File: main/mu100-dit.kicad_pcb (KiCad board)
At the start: 2 copper layers, 17.6 x 40 mm, 16 parts, among them J1 Conn_01x10_Female, U1 TOTX-177L, U2 AK4103A

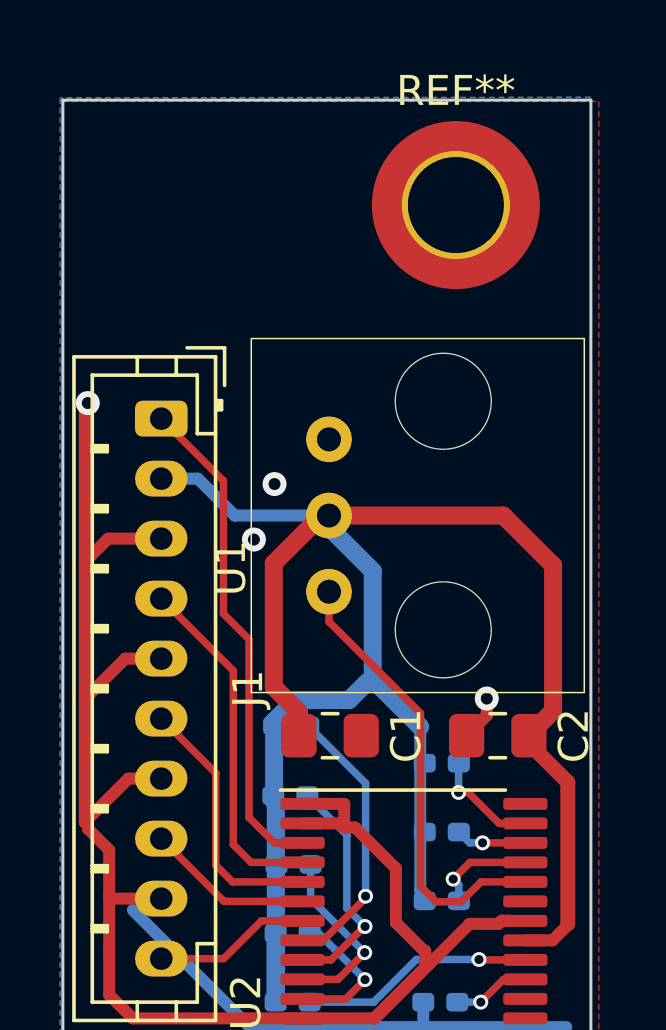
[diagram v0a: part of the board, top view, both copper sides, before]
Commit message: Add reset circuit, remove need for reset
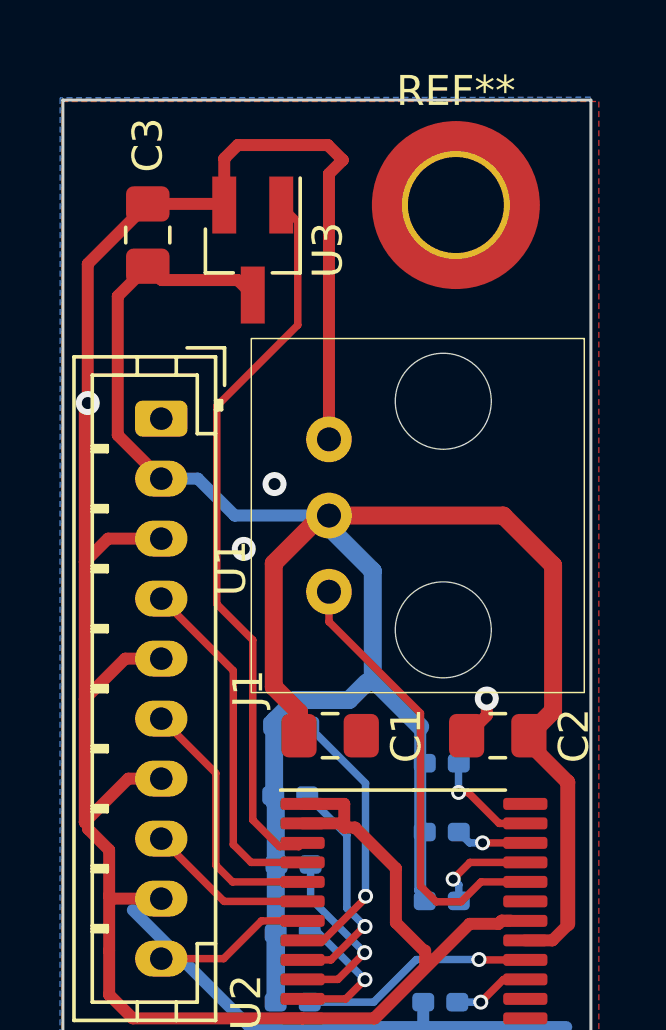
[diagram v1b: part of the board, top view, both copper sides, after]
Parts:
- added C3: 0.1u/35V, Capacitor_SMD:C_0805_2012Metric_Pad1.18x1.45mm_HandSolder, F.Cu at (46.5, 90.5)
- added U3: APX809S-46SR-7, Package_TO_SOT_SMD:SOT-23_Handsoldering, F.Cu at (50.0, 91.0)
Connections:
- J1 pad 1: /RESET -> unconnected-(J1-Pad1)
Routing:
- net GND: track 76.6 -> 107.3 mm
- net +5V: track 65.9 -> 77.9 mm
- net /RESET: track 16.6 -> 24.4 mm
- net /LRCK: track 5.23 -> 0.00 mm

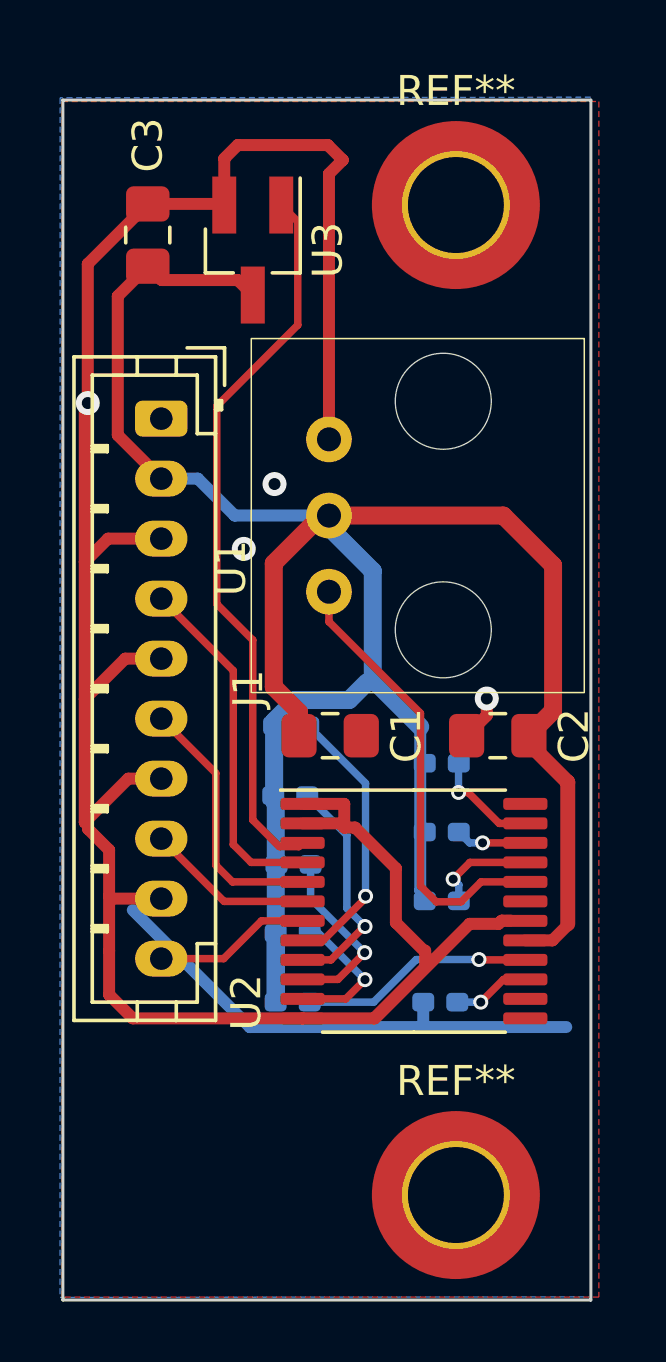
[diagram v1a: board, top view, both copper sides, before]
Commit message: Update screw hole position
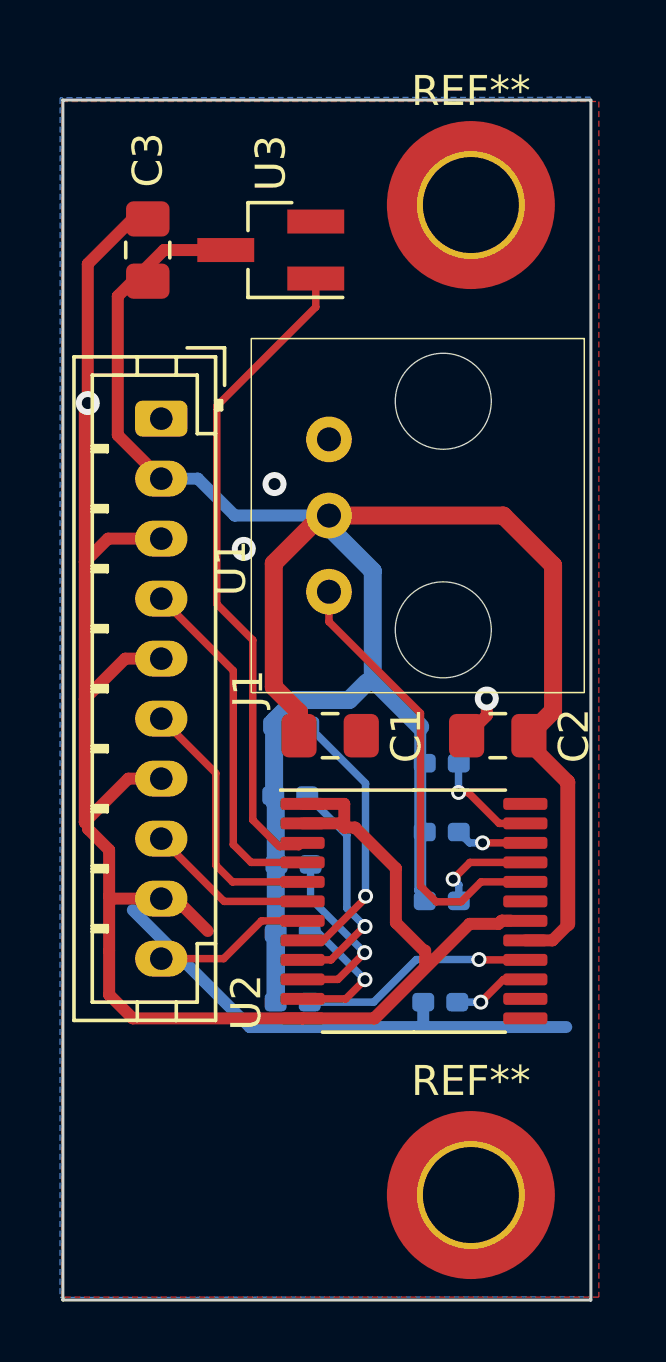
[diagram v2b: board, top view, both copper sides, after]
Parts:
- moved U3 0.60 mm to (50.6, 91.0), turned to 180 degrees
- moved C3 0.50 mm to (46.5, 91.0)
- moved REF** 0.50 mm to (57.3, 89.5)
- moved REF** 0.50 mm to (57.3, 122.5)
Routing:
- net GND: track 107.3 -> 91.0 mm
- net /RESET: track 24.4 -> 22.0 mm
- net +5V: track 77.9 -> 76.9 mm

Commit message: Move reset circuit to other side of board
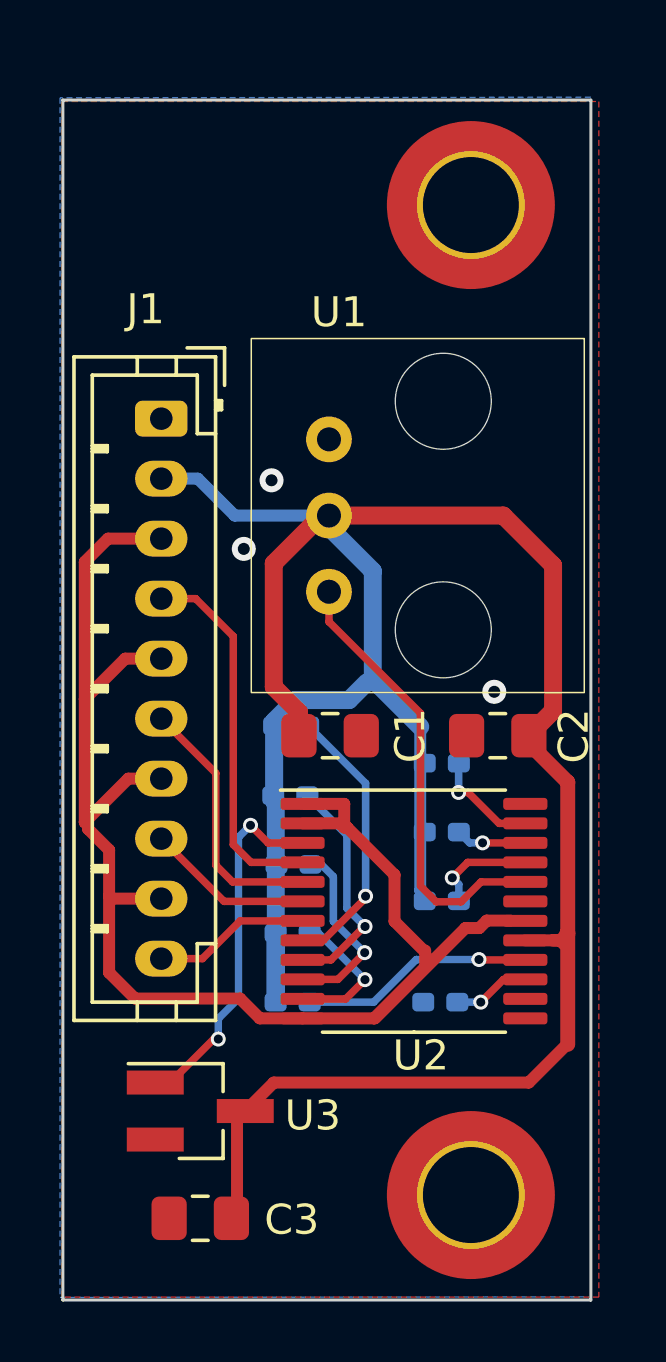
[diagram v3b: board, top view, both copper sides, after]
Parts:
- moved C3 32.3 mm to (48.2, 123.3), turned to 0 degrees
- moved U3 28.8 mm to (48.2, 119.7), turned to 0 degrees
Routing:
- net GND: track 91.0 -> 52.4 mm, vias 4 -> 3
- net +5V: track 76.9 -> 89.0 mm
- net /RESET: track 22.0 -> 12.2 mm, vias 0 -> 2
- net /LRCK: track 0.00 -> 5.23 mm
- net /MCLK: track 11.7 -> 12.4 mm

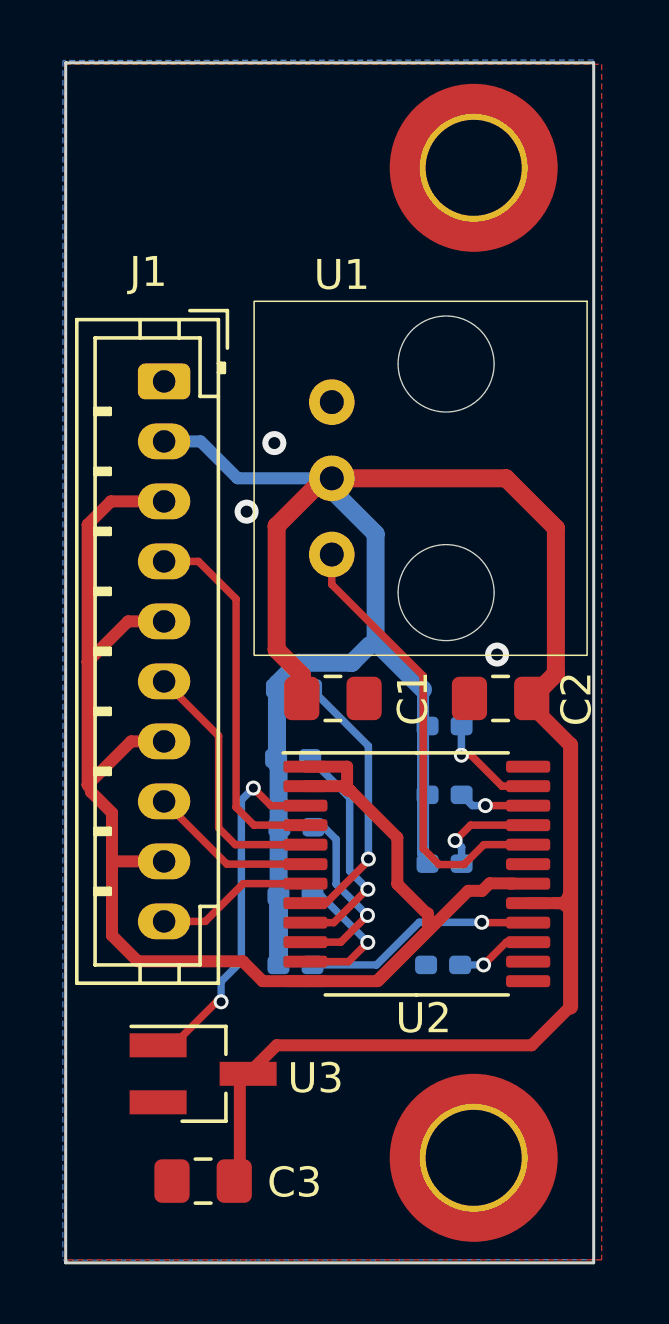
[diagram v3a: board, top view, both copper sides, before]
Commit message: Add header for optional coax output
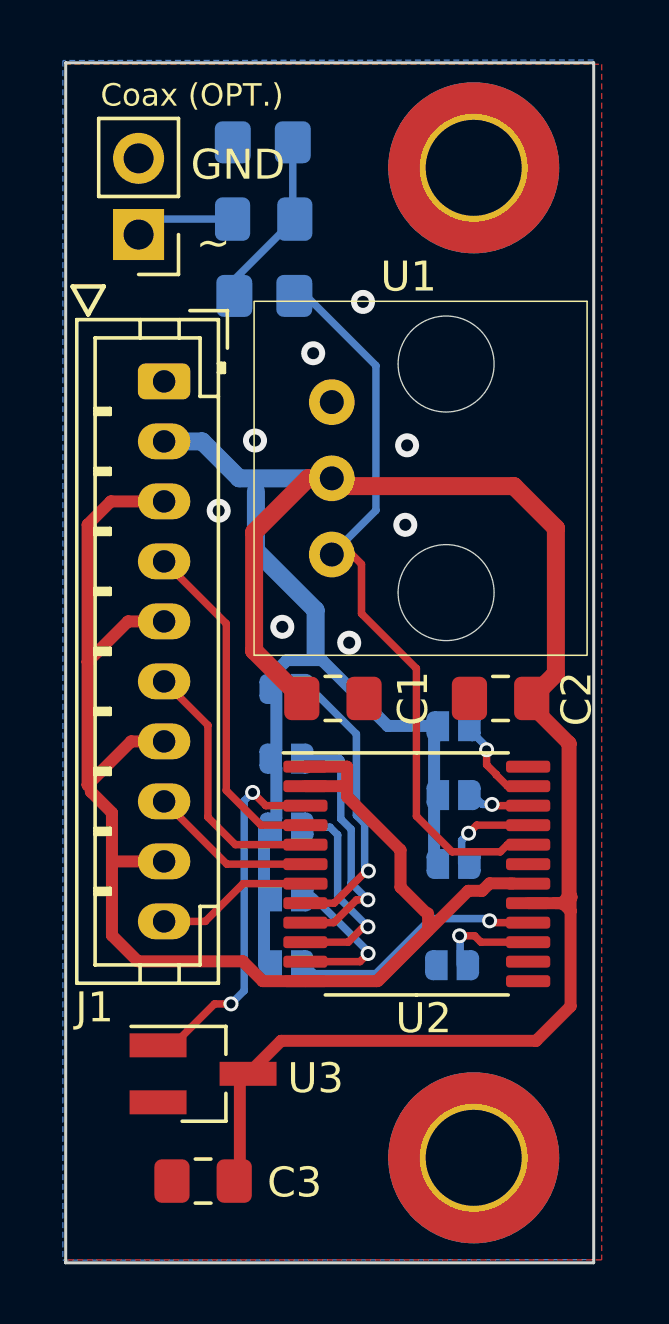
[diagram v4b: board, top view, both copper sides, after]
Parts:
- added C4: 0.1u/35V, Capacitor_SMD:C_0805_2012Metric_Pad1.18x1.45mm_HandSolder, B.Cu at (50.3, 91.2)
- added J2: Conn_01x02_Male, Connector_PinHeader_2.54mm:PinHeader_1x02_P2.54mm_Vertical, F.Cu at (46.1, 91.7)
- added R1: 330, Resistor_SMD:R_0805_2012Metric_Pad1.20x1.40mm_HandSolder, B.Cu at (50.3, 93.8)
- added R2: 100, Resistor_SMD:R_0805_2012Metric_Pad1.20x1.40mm_HandSolder, B.Cu at (50.2, 88.7)
- H1, H2: renamed from REF**; value MountingHole_3.2mm_M3_DIN965_Pad_TopOnly -> MountingHole_Pad; footprint MountingHole:MountingHole_3.2mm_M3_DIN965_Pad_TopOnly -> MountingHole:MountingHole_3.2mm_M3_ISO7380_Pad_TopBottom
- JP1, JP2, JP3, JP4, JP5, JP6, JP7, JP8, JP9: footprint Capacitor_SMD:C_0402_1005Metric_Pad0.74x0.62mm_HandSolder -> footprints:SolderJumper-Open_RoundedPad-custom
- moved JP3 0.33 mm to (51.0, 111.5)
- moved JP5 0.30 mm to (56.6, 112.7)
- moved JP6 0.30 mm to (56.6, 110.4)
- moved JP7 0.30 mm to (56.6, 108.1)
- moved JP4 0.30 mm to (51.0, 113.8)
- moved JP8 0.30 mm to (56.5, 116.1)
- moved JP9 0.30 mm to (51.0, 116.1)
- moved JP1 0.25 mm to (51.0, 106.9)
- moved JP2 0.22 mm to (51.0, 109.2)
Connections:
- H1 pad 1: (no net) -> GND
- H2 pad 1: (no net) -> GND
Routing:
- net /TXP: track 15.1 -> 25.2 mm
- net Net-(C4-Pad1): track 0.00 -> 5.98 mm
- net +5V: track 89.0 -> 85.0 mm
- net Net-(C4-Pad2): track 0.00 -> 3.54 mm
- net /MCLK: track 12.4 -> 11.6 mm
- net /FS1: track 7.70 -> 8.48 mm
- net /CKS0: track 2.58 -> 3.35 mm
- net /CKS1: track 7.78 -> 8.34 mm
- net GND: track 52.4 -> 52.2 mm, vias 3 -> 8
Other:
- board text added: "(▼)"
- board text added: "Coax (OPT.)"
- board text added: "github.com/ nikitalita/ MU100-DIT"
- board text added: "~"
- board text removed: "(PDWN)"
- board text removed: "~{RST}"

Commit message: combine pcb projects
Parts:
- added C5: 0.1u/35V, Capacitor_SMD:C_0805_2012Metric_Pad1.18x1.45mm_HandSolder, F.Cu at (61.7, 86.7)
- added J3: Conn_01x17_Male, Connector_PinHeader_2.00mm:PinHeader_1x17_P2.00mm_Vertical, F.Cu at (54.6, 83.8)
- added J4: 51247 Molex, Molex-52147-1710:Molex_Wire-Trap_52147-1710_1x17_P2.00mm_Vertical, B.Cu at (57.5, 83.8)
- added J5: JST-PH_01x10_Socket, Connector_JST:JST_PH_B10B-PH-K_1x10_P2.00mm_Vertical, B.Cu at (65.5, 108.8)
- added R3: 47, Resistor_SMD:R_0805_2012Metric_Pad1.20x1.40mm_HandSolder, F.Cu at (61.7, 103.1)
- added R4: 47, Resistor_SMD:R_0805_2012Metric_Pad1.20x1.40mm_HandSolder, F.Cu at (61.7, 99.3)
- added R5: 47, Resistor_SMD:R_0805_2012Metric_Pad1.20x1.40mm_HandSolder, F.Cu at (61.7, 95.4)
- added R6: 47, Resistor_SMD:R_0805_2012Metric_Pad1.20x1.40mm_HandSolder, F.Cu at (61.7, 91.6)
- moved J2 34.6 mm to (80.2, 85.7)
- moved JP5 34.6 mm to (90.7, 106.6)
- moved JP6 34.6 mm to (90.7, 104.4)
- moved JP7 34.6 mm to (90.7, 102.1)
- moved R1 34.6 mm to (84.4, 87.7)
- moved C1 34.6 mm to (86.7, 101.1)
- moved C2 34.6 mm to (92.2, 101.1)
- moved C3 34.6 mm to (82.3, 117.2)
- moved J1 34.6 mm to (81.0, 90.6)
- moved JP1 34.6 mm to (85.1, 100.8)
- moved JP2 34.6 mm to (85.1, 103.1)
- moved JP3 34.6 mm to (85.1, 105.4)
- moved JP4 34.6 mm to (85.1, 107.7)
- moved JP8 34.6 mm to (90.6, 110.0)
- moved JP9 34.6 mm to (85.1, 110.0)
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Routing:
- net +5V: track 85.0 -> 131.8 mm
- net /MU100-dit-connector-board/WCLK: track 0.00 -> 18.4 mm, vias 0 -> 1
- net /MU100-dit-connector-board/DACOL: track 0.00 -> 13.3 mm, vias 0 -> 1
- net /MU100-dit-connector-board/QCLK: track 0.00 -> 9.07 mm
- net /MU100-dit-connector-board/CK256: track 0.00 -> 6.33 mm
- net /MU100-dit-connector-board/BICK: track 0.00 -> 3.14 mm
- net Net-(J3-Pad6): track 0.00 -> 2.86 mm
- net Net-(J3-Pad10): track 0.00 -> 2.86 mm
- net GNDA: track 0.00 -> 2.86 mm
- net /MU100-dit-connector-board/SYOD: track 0.00 -> 2.86 mm
- net /MU100-dit-connector-board/RER: track 0.00 -> 2.86 mm
- net /MU100-dit-connector-board/REB: track 0.00 -> 2.86 mm
- net /MU100-dit-connector-board/REA: track 0.00 -> 2.86 mm
- net /MU100-dit-connector-board/MEL00: track 0.00 -> 2.86 mm
- net +9VA: track 0.00 -> 2.86 mm
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- added copper zone on B.Cu, net +5V
- added copper zone on F.Cu, net +5V
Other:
- board size 17.6 x 40 mm -> 42.8 x 40 mm
- board text added: "+9VA"
- board text added: "100"
- board text added: "47"
- board text added: "5V"
- board text added: "AGND"
- board text added: "CK256 (MCLK)"
- board text added: "DACOL (SDAT)"
- board text added: "MELO0"
- board text added: "MU90 only"
- board text added: "MU90/100R: Molex connector, populated resistors MU90/100: Unpopulated header, unpopulated resistors"
- board text added: "NC"
- board text added: "QCLK (BCK)"
- board text added: "REA"
- board text added: "REB"
- board text added: "RER"
- board text added: "SYOD"
- board text added: "TODO: Figure out how to fix ERC complaining about PWR and GND not connected between PCBs"
- board text added: "WCLK (LRCK)"

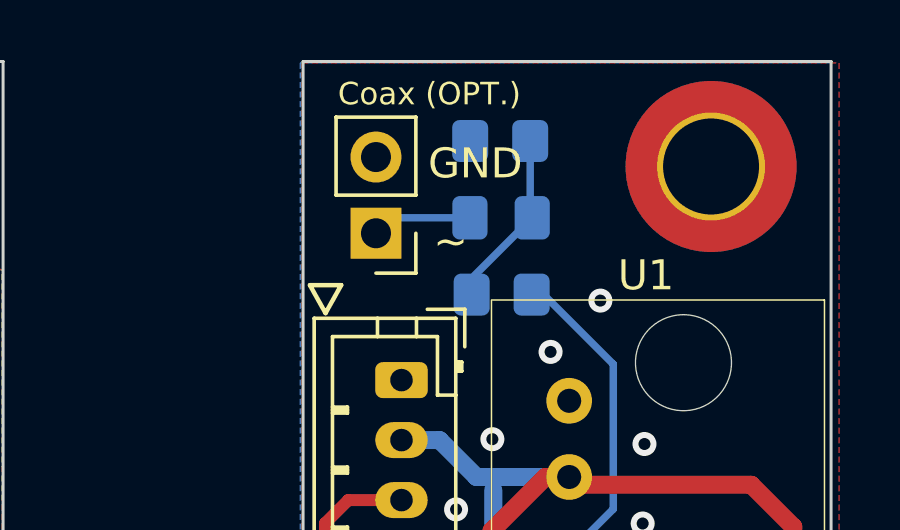
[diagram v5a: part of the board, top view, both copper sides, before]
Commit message: fix coax placement
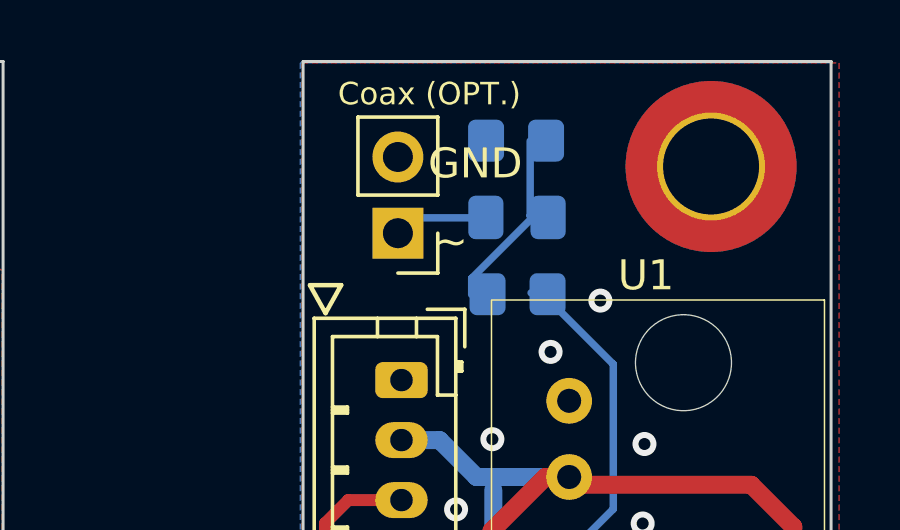
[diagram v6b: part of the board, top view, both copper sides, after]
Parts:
- moved J2 0.73 mm to (80.9, 85.7)
- moved C4 0.53 mm to (84.9, 85.2)
- moved R1 0.53 mm to (84.9, 87.7)
- moved R2 0.53 mm to (84.8, 82.6)
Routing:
- net Net-(C4-Pad2): track 3.54 -> 2.63 mm

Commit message: WIP
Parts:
- removed C5: 0.1u/35V, Capacitor_SMD:C_0805_2012Metric_Pad1.18x1.45mm_HandSolder
- removed J3: Conn_01x17_Male, Connector_PinHeader_2.00mm:PinHeader_1x17_P2.00mm_Vertical
- removed J4: 51247 Molex, Molex-52147-1710:Molex_Wire-Trap_52147-1710_1x17_P2.00mm_Vertical
- removed J5: JST-PH_01x10_Socket, Connector_JST:JST_PH_B10B-PH-K_1x10_P2.00mm_Vertical
- removed R3, R4, R5, R6: 47, Resistor_SMD:R_0805_2012Metric_Pad1.20x1.40mm_HandSolder
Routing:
- net +5V: track 131.8 -> 85.0 mm
- net /MU100-dit-connector-board/WCLK: track 18.4 -> 0.00 mm, vias 1 -> 0
- net /MU100-dit-connector-board/DACOL: track 13.3 -> 0.00 mm, vias 1 -> 0
- net /MU100-dit-connector-board/QCLK: track 9.07 -> 0.00 mm
- net /MU100-dit-connector-board/CK256: track 6.33 -> 0.00 mm
- net /MU100-dit-connector-board/BICK: track 3.14 -> 0.00 mm
- net Net-(J3-Pad6): track 2.86 -> 0.00 mm
- net Net-(J3-Pad10): track 2.86 -> 0.00 mm
- net GNDA: track 2.86 -> 0.00 mm
- net /MU100-dit-connector-board/SYOD: track 2.86 -> 0.00 mm
- net /MU100-dit-connector-board/RER: track 2.86 -> 0.00 mm
- net /MU100-dit-connector-board/REB: track 2.86 -> 0.00 mm
- net /MU100-dit-connector-board/REA: track 2.86 -> 0.00 mm
- net /MU100-dit-connector-board/MEL00: track 2.86 -> 0.00 mm
- net +9VA: track 2.86 -> 0.00 mm
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- removed copper zone on B.Cu, net +5V
- removed copper zone on F.Cu, net +5V
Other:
- board size 42.8 x 40 mm -> 17.6 x 40 mm
- board text removed: "+9VA"
- board text removed: "100"
- board text removed: "47"
- board text removed: "5V"
- board text removed: "AGND"
- board text removed: "CK256 (MCLK)"
- board text removed: "DACOL (SDAT)"
- board text removed: "MELO0"
- board text removed: "MU90 only"
- board text removed: "MU90/100R: Molex connector, populated resistors MU90/100: Unpopulated header, unpopulated resistors"
- board text removed: "QCLK (BCK)"
- board text removed: "REA"
- board text removed: "REB"
- board text removed: "RER"
- board text removed: "SYOD"
- board text removed: "TODO: Figure out how to fix ERC complaining about PWR and GND not connected between PCBs"
- board text removed: "WCLK (LRCK)"
